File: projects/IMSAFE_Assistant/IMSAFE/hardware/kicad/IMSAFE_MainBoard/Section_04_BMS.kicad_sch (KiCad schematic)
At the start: 0 parts

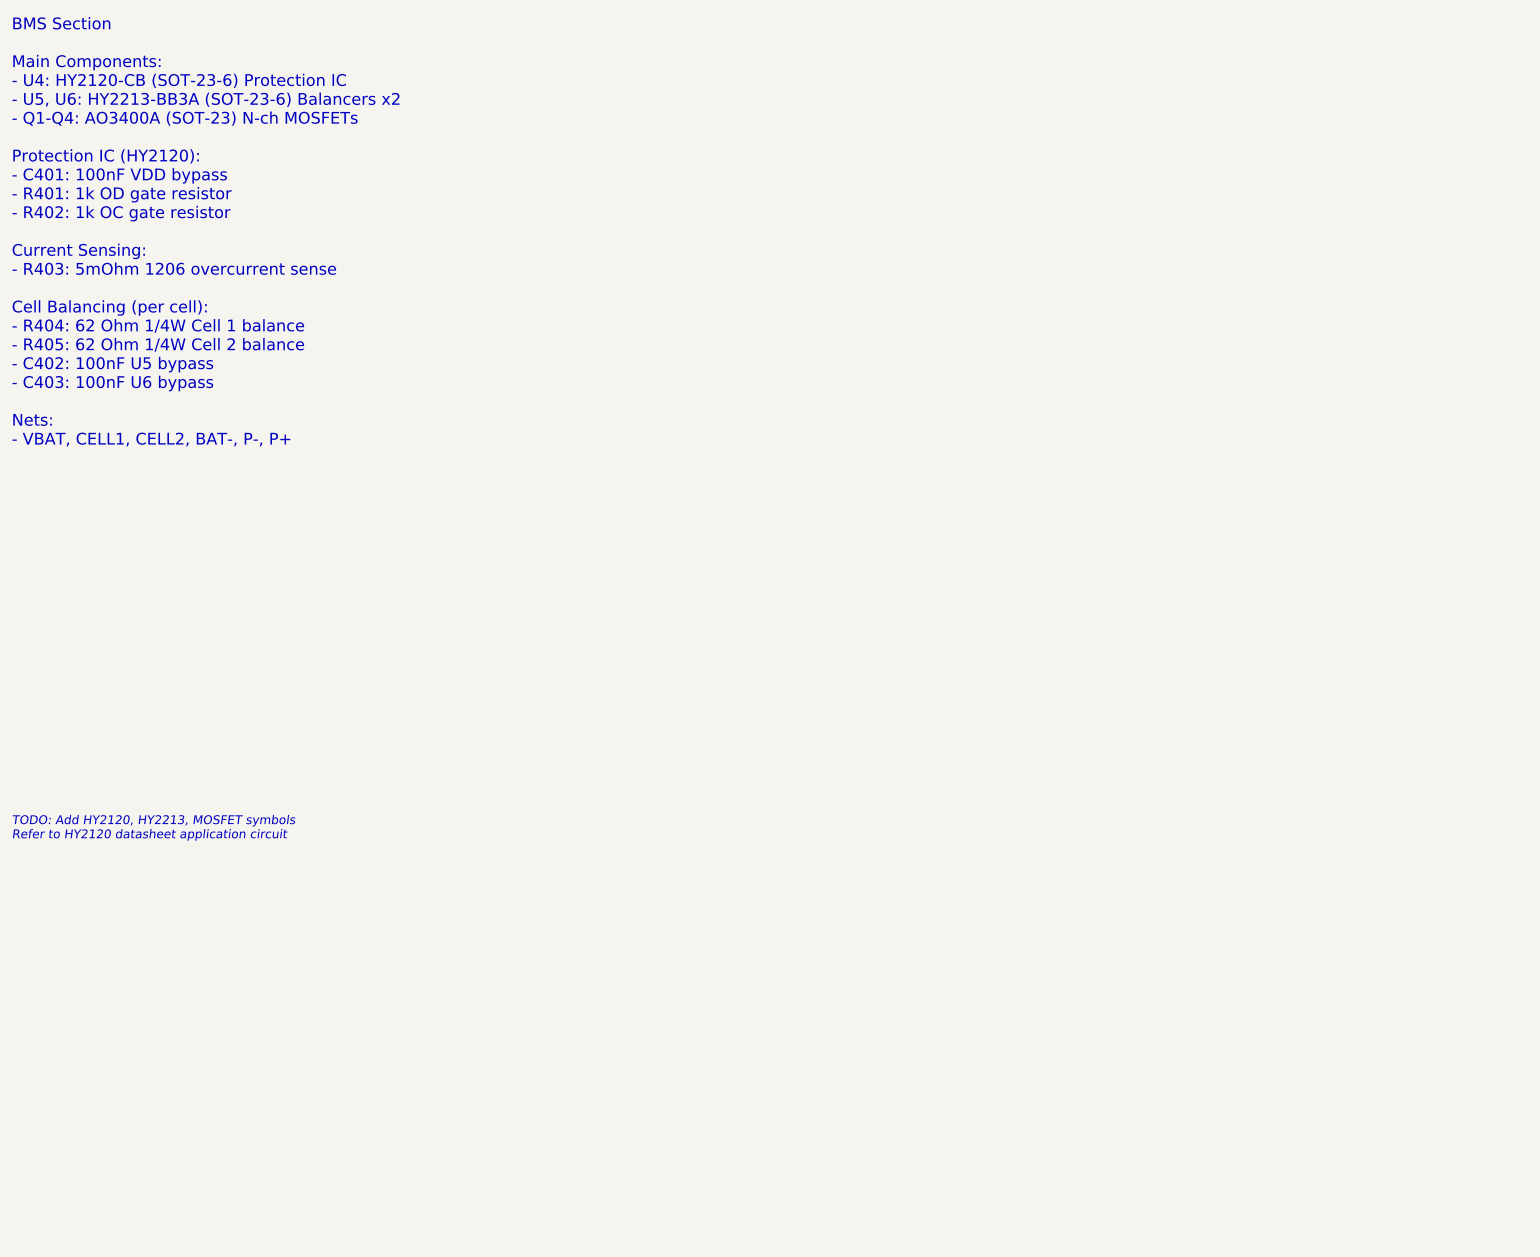
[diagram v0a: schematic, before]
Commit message: Add Section 04 BMS schematic with protection and balancing
BMS circuit features:
- HY2120-CB 2S protection IC (overcharge/overdischarge/overcurrent)
- HY2213-BB3A cell balancers (2x) with 62Ω bleed resistors
- AO3400A MOSFETs (4x) in back-to-back configuration
- 5mΩ current sense resistor (40A trip threshold)

Calculations added:
- Protection threshold analysis
- Current sense resistor sizing (200mV/40A = 5mΩ)
- Cell balancing resistor sizing (4.2V/68mA = 62Ω)
- MOSFET conduction loss analysis

Co-Authored-By: Claude Opus 4.5 <noreply@anthropic.com>
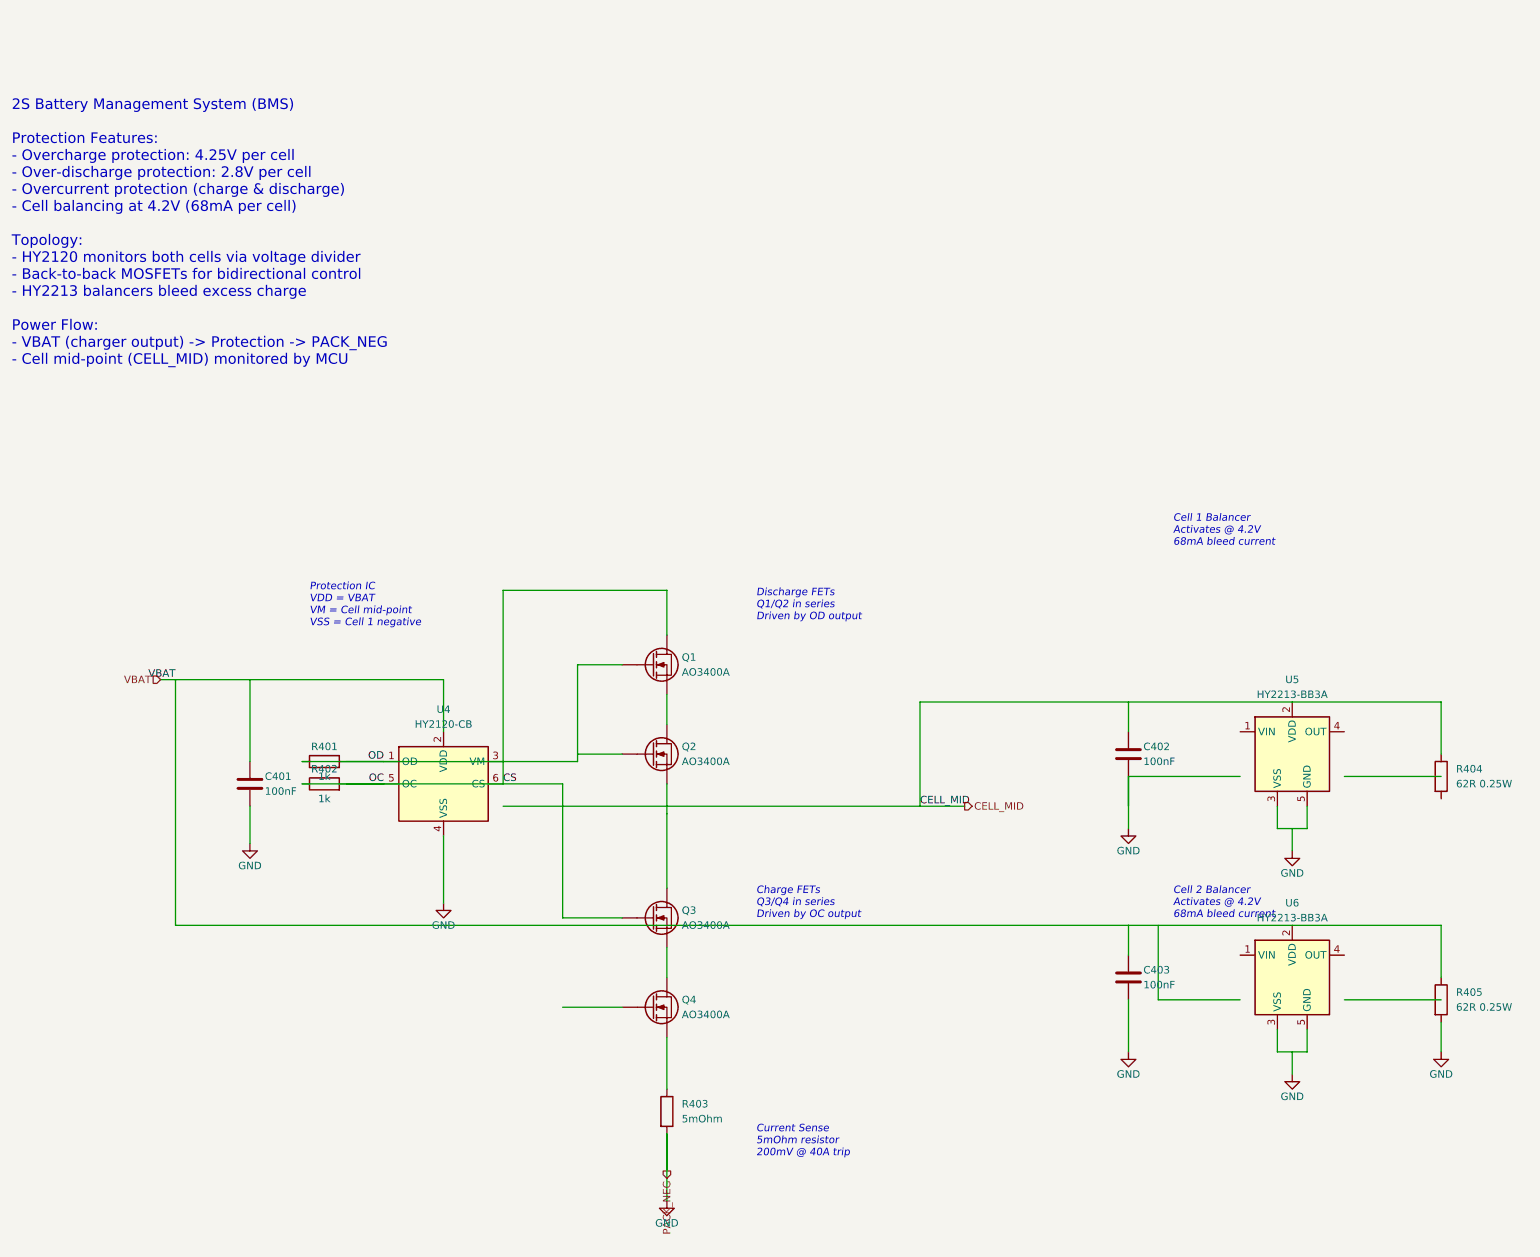
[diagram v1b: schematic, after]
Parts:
- added C401, C402, C403: 100nF, Capacitor_SMD:C_0603_1608Metric, symbol Device:C
- added Q1, Q2, Q3, Q4: AO3400A, Package_TO_SOT_SMD:SOT-23, symbol Device:Q_NMOS_GDS
- added R401, R402: 1k, Resistor_SMD:R_0603_1608Metric, symbol Device:R
- added R403: 5mOhm, Resistor_SMD:R_1206_3216Metric, symbol Device:R
- added R404, R405: 62R 0.25W, Resistor_SMD:R_0805_2012Metric, symbol Device:R
- added U4: HY2120-CB, Package_TO_SOT_SMD:SOT-23-6, symbol BMS:HY2120-CB
- added U5, U6: HY2213-BB3A, Package_TO_SOT_SMD:SOT-23-6, symbol BMS:HY2213-BB3A
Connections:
- new net: Q1.3 (S), Q2.2 (D)
- new net: Q2.3 (S), Q3.2 (D)
- new net: Q3.3 (S), Q4.2 (D)
- new net: Q4.3 (S), R403.1
- new net: U5.3 (VSS), U5.5 (GND)
- new net: U6.3 (VSS), U6.5 (GND)
- new net CELL_MID: R404.1, U5.2 (VDD)
- new net CS: Q3.1 (G), R402.1, R402.2, U4.5 (OC), U4.6 (CS)
- new net GND: C401.2, C402.2, C403.2, R403.2, R405.2, U4.4 (VSS)
- new net OD: Q1.1 (G), R401.1, R401.2, U4.1 (OD)
- new net VBAT: C403.1, R405.1, U4.2 (VDD), U6.2 (VDD)
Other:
- note added: "2S Battery Management System (BMS) Protection Features: - Overcharge protection: 4.25V per cell - Over-discharge protection: 2.8V per cell - Overcurrent protection (charge & discharge) - Cell balancing at 4.2V (68mA per cell) Topology: - HY2120 monitors both cells via voltage divider - Back-to-back MOSFETs for bidirectional control - HY2213 balancers bleed excess charge Power Flow: - VBAT (charge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"
- note added: "Cell 1 Balancer Activates @ 4.2V 68mA bleed current"
- note added: "Cell 2 Balancer Activates @ 4.2V 68mA bleed current"
- note added: "Charge FETs Q3/Q4 in series Driven by OC output"
- note added: "Current Sense 5mOhm resistor 200mV @ 40A trip"
- note added: "Discharge FETs Q1/Q2 in series Driven by OD output"
- note added: "Protection IC VDD = VBAT VM = Cell mid-point VSS = Cell 1 negative"
- note removed: "BMS Section Main Components: - U4: HY2120-CB (SOT-23-6) Protection IC - U5, U6: HY2213-BB3A (SOT-23-6) Balancers x2 - Q1-Q4: AO3400A (SOT-23) N-ch MOSFETs Protection IC (HY2120): - C401: 100nF VDD bypass - R401: 1k OD gate resistor - R402: 1k OC gate resistor Current Sensing: - R403: 5mOhm 1206 overcurrent sense Cell Balancing (per cell): - R404: 62 Ohm 1/4W Cell 1 balance - R405: 62 Ohm 1/4W Cel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"
- note removed: "TODO: Add HY2120, HY2213, MOSFET symbols Refer to HY2120 datasheet application circuit"

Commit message: Fix Section 06 FB divider for correct 5V output
- Change R602 from 24.3k to 19.1k (JLCPCB C25947)
- Corrects output voltage from 4.09V to 5.03V
- Update schematic text annotations with correct calculations
- Update design-rationale.md to reflect the fix
- Add PWR_FLAG symbols to Sections 04, 05, 06 for ERC compliance

Co-Authored-By: Claude Opus 4.5 <noreply@anthropic.com>
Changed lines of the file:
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@@
 	(wire (pts (xy 180.34 123.19) (xy 187.96 123.19)) (stroke (width 0) (type default)) (uuid "w-hl-cellmid"))
 	(wire (pts (xy 137.16 179.07) (xy 137.16 185.42)) (stroke (width 0) (type default)) (uuid "w-hl-packneg"))
+	(symbol (lib_id "power:PWR_FLAG") (at 60.96 101.6 0) (unit 1)
+		(exclude_from_sim no) (in_bom yes) (on_board yes) (dnp no)
+		(uuid "pwr-flag-vbat-04")
+		(property "Reference" "#FLG0401" (at 60.96 99.695 0) (effects (font (size 1.27 1.27)) hide))
+		(property "Value" "PWR_FLAG" (at 60.96 97.79 0) (effects (font (size 1.27 1.27))))
+		(property "Footprint" "" (at 60.96 101.6 0) (effects (font (size 1.27 1.27)) hide))
+		(property "Datasheet" "~" (at 60.96 101.6 0) (effects (font (size 1.27 1.27)) hide))
+		(pin "1" (uuid "pwr-flag-vbat-04-p1"))
+		(instances (project "IMSAFE_MainBoard" (path "/sec04-0001-0002-0003-000000000001" (reference "#FLG0401") (unit 1))))
+	)
 	(sheet_instances (path "/" (page "1")))
 )

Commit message: Fix ERC errors across multiple schematic sections
- Section_04_BMS: Add VSYS hierarchical label for root schematic connection
- Section_05/06 Regulators: Add PWR_FLAG wire and junction to VSYS net
- Section_07_Barometric: Connect BMP390 SCK pin to GND for I2C mode
- Section_14_IO_Expander: Add no-connect symbols for unused MCP23017 GPIO pins
- Update design-rationale.md with ERC remediation status

Co-Authored-By: Claude Opus 4.5 <noreply@anthropic.com>
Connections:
- net VSYS: now reaches Q2.3 (S), Q3.2 (D)
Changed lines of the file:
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@@
 		(uuid "hl-packneg")
+	)
+	(hierarchical_label "VSYS" (shape output) (at 144.78 124.46 0) (fields_autoplaced yes)
+		(effects (font (size 1.27 1.27)) (justify left))
+		(uuid "hl-vsys")
 	)
 	(wire (pts (xy 50.8 101.6) (xy 53.34 101.6)) (stroke (width 0) (type default)) (uuid "w-hl-vbat"))
 	(wire (pts (xy 180.34 123.19) (xy 187.96 123.19)) (stroke (width 0) (type default)) (uuid "w-hl-cellmid"))
 	(wire (pts (xy 137.16 179.07) (xy 137.16 185.42)) (stroke (width 0) (type default)) (uuid "w-hl-packneg"))
+	(wire (pts (xy 137.16 124.46) (xy 144.78 124.46)) (stroke (width 0) (type default)) (uuid "w-hl-vsys"))
+	(label "VSYS" (at 140.97 124.46 0) (fields_autoplaced yes)
+		(effects (font (size 1.27 1.27)) (justify left bottom))
+		(uuid "label-vsys")
+	)
 	(symbol (lib_id "power:PWR_FLAG") (at 60.96 101.6 0) (unit 1)
 		(exclude_from_sim no) (in_bom yes) (on_board yes) (dnp no)

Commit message: Add sensor and interface schematic implementations
- Section 01: MCU Core additional connections
- Section 04: BMS refinements
- Section 07: Barometric sensor (BMP390)
- Section 08: IMU (ICM-42688-P) full implementation
- Section 09: Magnetometer (MMC5983MA) full implementation
- Section 10: Gas sensor (MICS-4514) with heater control
- Section 11: Temp/Humidity (Si7021-A20) implementation
- Section 14: I/O Expander updates
- Section 16: Rotary encoder connections
- Section 19: Audio buzzer (MLT-8530) with MOSFET driver

Co-Authored-By: Claude Opus 4.5 <noreply@anthropic.com>
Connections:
- net CS: now also Q4.1 (G)
- net GND: now also U5.3 (VSS), U5.5 (GND)
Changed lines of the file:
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@@
 	(wire (pts (xy 119.38 119.38) (xy 119.38 142.24)) (stroke (width 0) (type default)) (uuid "w-oc-gate-1"))
 	(wire (pts (xy 119.38 142.24) (xy 129.54 142.24)) (stroke (width 0) (type default)) (uuid "w-oc-gate-q3"))
+	(wire (pts (xy 119.38 142.24) (xy 119.38 157.48)) (stroke (width 0) (type default)) (uuid "w-oc-gate-down"))
 	(wire (pts (xy 119.38 157.48) (xy 129.54 157.48)) (stroke (width 0) (type default)) (uuid "w-oc-gate-q4"))
 	(wire (pts (xy 137.16 94.0) (xy 137.16 86.36)) (stroke (width 0) (type default)) (uuid "w-q1-drain-1"))
@@
 	(wire (pts (xy 246.38 123.19) (xy 246.38 127)) (stroke (width 0) (type default)) (uuid "w-u5-gnd"))
 	(wire (pts (xy 241.3 123.19) (xy 241.3 127)) (stroke (width 0) (type default)) (uuid "w-u5-vss"))
-	(wire (pts (xy 241.3 127) (xy 246.38 127)) (stroke (width 0) (type default)) (uuid "w-u5-gnd-join"))
+	(wire (pts (xy 241.3 127) (xy 243.84 127)) (stroke (width 0) (type default)) (uuid "w-u5-gnd-join-1"))
+	(wire (pts (xy 243.84 127) (xy 246.38 127)) (stroke (width 0) (type default)) (uuid "w-u5-gnd-join-2"))
 	(wire (pts (xy 243.84 127) (xy 243.84 130.81)) (stroke (width 0) (type default)) (uuid "w-u5-gnd-ext"))
+	(junction (at 243.84 127) (diameter 0) (color 0 0 0 0) (uuid "junc-u5-gnd"))
 	(wire (pts (xy 246.38 161.29) (xy 246.38 165.1)) (stroke (width 0) (type default)) (uuid "w-u6-gnd"))
 	(wire (pts (xy 241.3 161.29) (xy 241.3 165.1)) (stroke (width 0) (type default)) (uuid "w-u6-vss"))

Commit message: Resolve Phase 2 design review items
Design decisions applied:
- I²C pull-ups: Keep 4.7kΩ (100kHz acceptable)
- USB: Document as FS-only (12 Mbps)
- BMS balancer: Upgrade R404/R405 to 1206 0.5W (C137556)

Updated IMSAFE-Phase2-Review-Notes.md with resolutions.

Co-Authored-By: Claude Opus 4.5 <noreply@anthropic.com>
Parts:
- R404, R405: value 62R 0.25W -> 62R 0.5W; footprint Resistor_SMD:R_0805_2012Metric -> Resistor_SMD:R_1206_3216Metric; JLCPCB C17828 -> C137556
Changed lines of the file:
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@@
 		(uuid "r404-uuid")
 		(property "Reference" "R404" (at 271.78 116.84 0) (effects (font (size 1.27 1.27)) (justify left)))
-		(property "Value" "62R 0.25W" (at 271.78 119.38 0) (effects (font (size 1.27 1.27)) (justify left)))
-		(property "Footprint" "Resistor_SMD:R_0805_2012Metric" (at 267.462 118.11 90) (effects (font (size 1.27 1.27)) hide))
+		(property "Value" "62R 0.5W" (at 271.78 119.38 0) (effects (font (size 1.27 1.27)) (justify left)))
+		(property "Footprint" "Resistor_SMD:R_1206_3216Metric" (at 267.462 118.11 90) (effects (font (size 1.27 1.27)) hide))
 		(property "Datasheet" "~" (at 269.24 118.11 0) (effects (font (size 1.27 1.27)) hide))
-		(property "JLCPCB" "C17828" (at 269.24 118.11 0) (effects (font (size 1.27 1.27)) hide))
+		(property "JLCPCB" "C137556" (at 269.24 118.11 0) (effects (font (size 1.27 1.27)) hide))
 		(pin "1" (uuid "r404-p1")) (pin "2" (uuid "r404-p2"))
 		(instances (project "IMSAFE_MainBoard" (path "/sec04-0001-0002-0003-000000000001" (reference "R404") (unit 1))))
@@
 		(uuid "r405-uuid")
 		(property "Reference" "R405" (at 271.78 154.94 0) (effects (font (size 1.27 1.27)) (justify left)))
-		(property "Value" "62R 0.25W" (at 271.78 157.48 0) (effects (font (size 1.27 1.27)) (justify left)))
-		(property "Footprint" "Resistor_SMD:R_0805_2012Metric" (at 267.462 156.21 90) (effects (font (size 1.27 1.27)) hide))
+		(property "Value" "62R 0.5W" (at 271.78 157.48 0) (effects (font (size 1.27 1.27)) (justify left)))
+		(property "Footprint" "Resistor_SMD:R_1206_3216Metric" (at 267.462 156.21 90) (effects (font (size 1.27 1.27)) hide))
 		(property "Datasheet" "~" (at 269.24 156.21 0) (effects (font (size 1.27 1.27)) hide))
-		(property "JLCPCB" "C17828" (at 269.24 156.21 0) (effects (font (size 1.27 1.27)) hide))
+		(property "JLCPCB" "C137556" (at 269.24 156.21 0) (effects (font (size 1.27 1.27)) hide))
 		(pin "1" (uuid "r405-p1")) (pin "2" (uuid "r405-p2"))
 		(instances (project "IMSAFE_MainBoard" (path "/sec04-0001-0002-0003-000000000001" (reference "R405") (unit 1))))
